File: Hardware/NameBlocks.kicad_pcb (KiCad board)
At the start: 2 copper layers, 0 parts

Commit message: Finished all footprints. Time for layout!
And I double checked the LED display footprint. Miraculous!
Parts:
- added BT1: Battery_Cell, Battery_Holders:Keystone_1058_1x2032-CoinCell, F.Cu at (25.2, -5.36)
- added C1: 0.1u, Capacitors_SMD:C_1206_HandSoldering, F.Cu at (0.00, 0.00)
- added J1: CONN_01X06, Socket_Strips:Socket_Strip_Angled_1x06_Pitch2.54mm, F.Cu at (-21.0, 30.7)
- added J2, J3: CONN_01X05, Socket_Strips:Socket_Strip_Angled_1x05_Pitch2.54mm, F.Cu at (0.00, 0.00)
- added Q1: Q_NMOS_GSD, TO_SOT_Packages_SMD:SC-59_Handsoldering, F.Cu at (0.00, 0.00)
- added R1, R2, R4: 1k, Resistors_SMD:R_1206_HandSoldering, F.Cu at (0.00, 0.00)
- added R3, R5, R6: 1M, Resistors_SMD:R_1206_HandSoldering, F.Cu at (0.00, 0.00)
- added RN1, RN2: 180, Housings_SSOP:SSOP-16_3.9x4.9mm_Pitch0.635mm, F.Cu at (0.00, 0.00)
- added S1: Button, Buttons_Switches_SMD:SW_SPST_PTS645, F.Cu at (6.82, -18.2)
- added TP1: TEST, Wire_Pads:SolderWirePad_single_1mmDrill, F.Cu at (0.00, 0.00)
- added U1: ACPSA04-41SRWA-17406, ACPSA04_Alphanumeric_LED, F.Cu at (29.1, 16.1)
- added U2: ATTiny828, Housings_QFP:TQFP-32_7x7mm_Pitch0.8mm, F.Cu at (-17.0, -8.66)
- added U3: MAX16054, TO_SOT_Packages_SMD:SOT-23-6_Handsoldering, F.Cu at (0.00, 0.00)
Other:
- board text added: "Winter 2017-2018"
- board text removed: "Winter 2017"

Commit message: Started layout. What a mess!
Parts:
- removed R3: 1M, Resistors_SMD:R_1206_HandSoldering
- removed TP1: TEST, Wire_Pads:SolderWirePad_single_1mmDrill
- BT1: footprint Battery_Holders:Keystone_1058_1x2032-CoinCell -> Battery_Holders:CR2032_SMD_BatteryHolder_BU2032SM-BT-GTR; moved to B.Cu
- C1: footprint Capacitors_SMD:C_1206_HandSoldering -> Capacitors_SMD:C_0805_HandSoldering
- Q1, U3: moved to B.Cu
- R1, R2, R4, R5, R6: footprint Resistors_SMD:R_1206_HandSoldering -> Resistors_SMD:R_0805_HandSoldering
- U1: footprint ACPSA04_Alphanumeric_LED -> ACPSA04_Alphanumeric_LED:ACPSA04_Alphanumeric_LED
- moved R4 149.6 mm to (132.2, 70.1), turned to 180 degrees
- moved R2 147.9 mm to (132.1, 66.5), turned to 180 degrees
- moved R1 146.3 mm to (132.1, 62.9), turned to 180 degrees
- moved U2 145.8 mm to (108.0, 66.2), turned to 270 degrees
- moved RN2 131.1 mm to (106.6, 76.3)
- moved J3 127.3 mm to (112.9, 58.9), turned to 180 degrees
- moved C1 125.6 mm to (99.1, 77.3), turned to 180 degrees
- moved J1 124.0 mm to (102.1, 44.7), turned to 270 degrees
- moved S1 121.1 mm to (83.3, 75.7), turned to 180 degrees
- moved RN1 119.4 mm to (106.6, 53.8)
- moved Q1 108.1 mm to (96.0, 49.7)
- moved R5 105.2 mm to (86.2, 60.2), turned to 180 degrees
- moved R6 103.1 mm to (86.2, 56.6), turned to 180 degrees
- moved U3 100.5 mm to (86.4, 51.5)
- moved J2 93.2 mm to (79.3, 49.0)
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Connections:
- J2 pad 2: /Signal_C0 -> /Signal_In_C3
- J2 pad 3: /Signal_C1 -> /Signal_In_C4
- J2 pad 4: /Signal_C2 -> /Signal_In_C5
- R1 pad 2: /Signal_C0 -> /Signal_Out_C0
- R2 pad 2: /Signal_C1 -> /Signal_Out_C1
- R4 pad 2: /Signal_C2 -> /Signal_Out_C2
- S1 pad 3: (no net) -> /Button
- S1 pad 4: (no net) -> /Button
- U2 pad 1: /Signal_C2 -> /Signal_Out_C2
- U2 pad 2: (no net) -> /Signal_In_C3
- U2 pad 3: (no net) -> /Signal_In_C4
- U2 pad 31: /Signal_C0 -> /Signal_Out_C0
- U2 pad 32: /Signal_C1 -> /Signal_Out_C1
- U2 pad 6: (no net) -> /Signal_In_C5
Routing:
- net /Button: track 0.00 -> 42.7 mm
- net Net-(RN2-Pad2): track 0.00 -> 28.1 mm, vias 0 -> 2
- net Net-(RN2-Pad1): track 0.00 -> 25.3 mm, vias 0 -> 2
- net Net-(RN1-Pad4): track 0.00 -> 19.5 mm
- net Net-(RN1-Pad3): track 0.00 -> 19.4 mm
- net Net-(RN1-Pad5): track 0.00 -> 19.4 mm
- net Net-(RN1-Pad15): track 0.00 -> 18.5 mm, vias 0 -> 2
- net VCC: track 0.00 -> 17.8 mm
- net Net-(RN1-Pad10): track 0.00 -> 17.2 mm, vias 0 -> 2
- net Net-(RN1-Pad14): track 0.00 -> 17.2 mm, vias 0 -> 2
- net Net-(RN1-Pad11): track 0.00 -> 16.6 mm, vias 0 -> 2
- net Net-(RN1-Pad12): track 0.00 -> 16.4 mm, vias 0 -> 2
- net Net-(RN1-Pad9): track 0.00 -> 16.4 mm, vias 0 -> 2
- net Net-(RN1-Pad13): track 0.00 -> 16.1 mm, vias 0 -> 2
- net Net-(RN2-Pad6): track 0.00 -> 16.0 mm
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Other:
- board outline added: 38.1 x 38.1 mm
- net class Default: clearance 0.2 -> 0.1524; trace_width 0.25 -> 0.1524; via_dia 0.6 -> 0.508; via_drill 0.4 -> 0.254
- net class Power added: clearance 0.1524, trace_width 0.254, via_dia 0.508, via_drill 0.254
- rule trace_clearance: 0.2 -> 0.1524
- rule trace_min: 0.2 -> 0.1524
- rule via_min_drill: 0.3 -> 0.254
- rule via_min_size: 0.4 -> 0.508

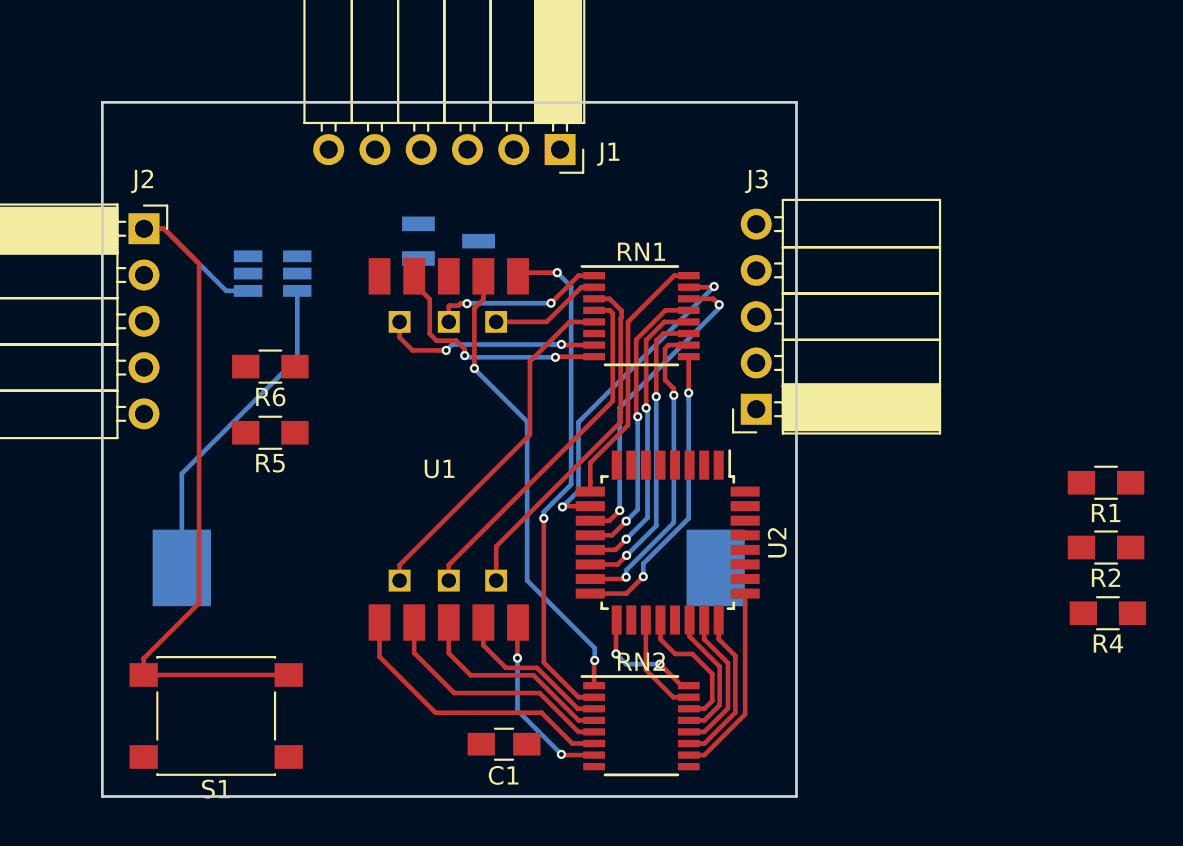
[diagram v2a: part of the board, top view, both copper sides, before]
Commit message: Layout finished, but need silkscreen. Going to ask about mfg-ability
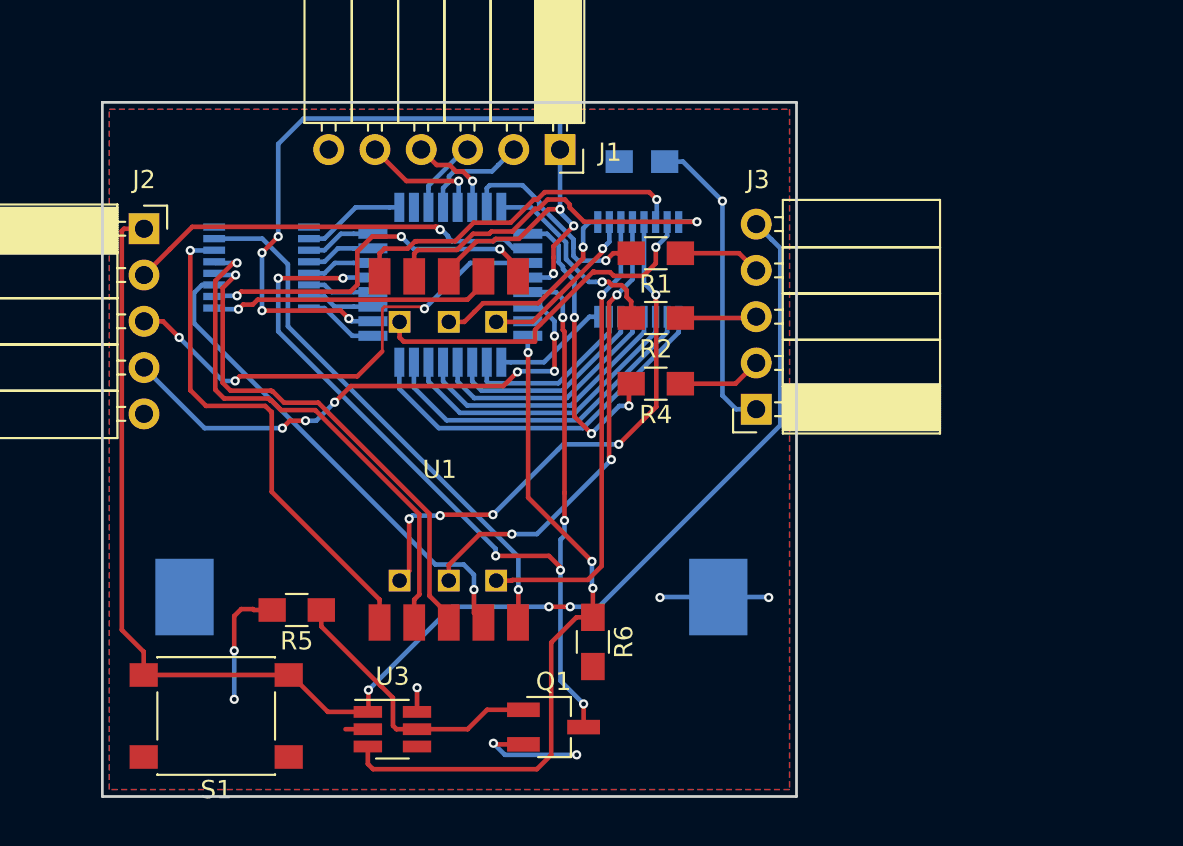
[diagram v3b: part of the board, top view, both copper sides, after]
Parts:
- C1, RN1, RN2, U2: moved to B.Cu
- Q1, U3: moved to F.Cu
- moved C1 32.9 mm to (106.6, 45.3), turned to 0 degrees
- moved RN2 32.7 mm to (85.8, 51.1)
- moved R4 27.8 mm to (107.4, 57.5)
- moved R1 27.7 mm to (107.4, 50.3)
- moved R2 27.7 mm to (107.4, 53.9)
- moved Q1 27.3 mm to (101.8, 76.4)
- moved U3 25.9 mm to (92.9, 76.5)
- moved R6 23.3 mm to (103.9, 71.7), turned to 270 degrees
- moved U2 18.5 mm to (96.1, 52.1), turned to 180 degrees
- moved R5 9.84 mm to (87.7, 69.9)
- moved RN1 2.57 mm to (106.4, 51.2), turned to 270 degrees
- moved BT1 1.61 mm to (81.5, 69.2)
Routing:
- net /uC_gnd: track 0.00 -> 55.6 mm, vias 0 -> 7
- net /Button: track 42.7 -> 80.7 mm, vias 0 -> 3
- net GND: track 0.00 -> 37.5 mm, vias 0 -> 7
- net /PowerOFF: track 0.00 -> 37.0 mm, vias 0 -> 3
- net VCC: track 17.8 -> 51.7 mm, vias 0 -> 8
- net /Signal_In_C5: track 0.00 -> 29.7 mm, vias 0 -> 6
- net /Signal_In_C4: track 0.00 -> 26.6 mm, vias 0 -> 3
- net /Signal_In_C3: track 0.00 -> 23.0 mm, vias 0 -> 1
- net Net-(RN2-Pad7): track 10.1 -> 29.5 mm, vias 2 -> 1
- net Net-(RN1-Pad6): track 0.00 -> 19.3 mm, vias 0 -> 1
- net Net-(RN2-Pad3): track 8.77 -> 26.9 mm, vias 0 -> 1
- net /Signal_Out_C2: track 0.00 -> 17.0 mm, vias 0 -> 3
- net Net-(RN2-Pad4): track 11.6 -> 28.2 mm, vias 0 -> 1
- net Net-(Q1-Pad1): track 0.00 -> 15.7 mm
- net Net-(RN2-Pad5): track 13.7 -> 28.9 mm, vias 0 -> 1
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- added copper zone on F.Cu, net GND
- added copper zone on B.Cu, net VCC

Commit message: Silkscreen done, ready for order
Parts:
- added G***: LOGO, KNEK-TEK_logo:KNEK-TEK_logo_9mm, F.Cu at (85.7, 51.2)
- added REF***: OSHW-Logo_5.7x6mm_SilkScreen, Symbols:OSHW-Logo_5.7x6mm_SilkScreen, F.Cu at (110.5, 75.7)
- R5: 1MΩ: renamed from R5
- R6: 1MΩ: renamed from R6
- moved J3 0.25 mm to (112.9, 59.2)
- moved U1 0.05 mm to (91.8, 51.6)
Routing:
- net Net-(RN2-Pad3): track 26.9 -> 26.1 mm
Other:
- board text added: "Feb 2018, v1.0"
- board text added: "GND"
- board text added: "VCC"
- board text added: "github.com/Erik-k/NameBlocks"
